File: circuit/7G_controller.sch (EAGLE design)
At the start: 21 parts, among them Q1 32768Hz, T1 TPS1101D

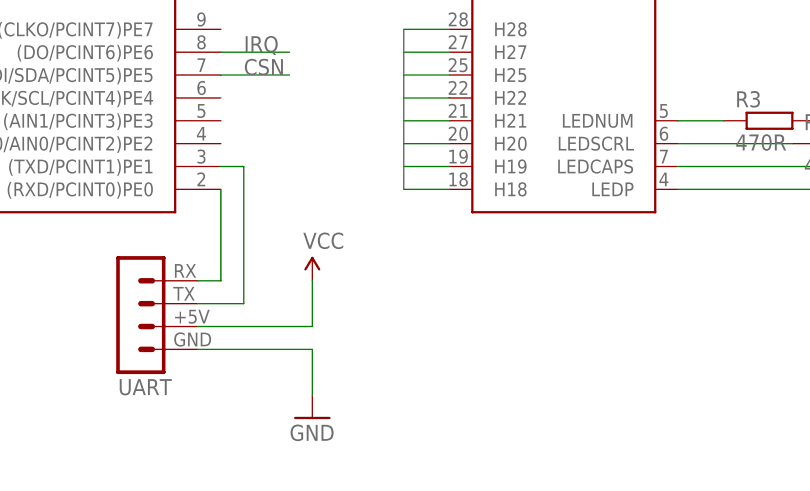
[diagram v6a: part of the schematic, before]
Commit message: 
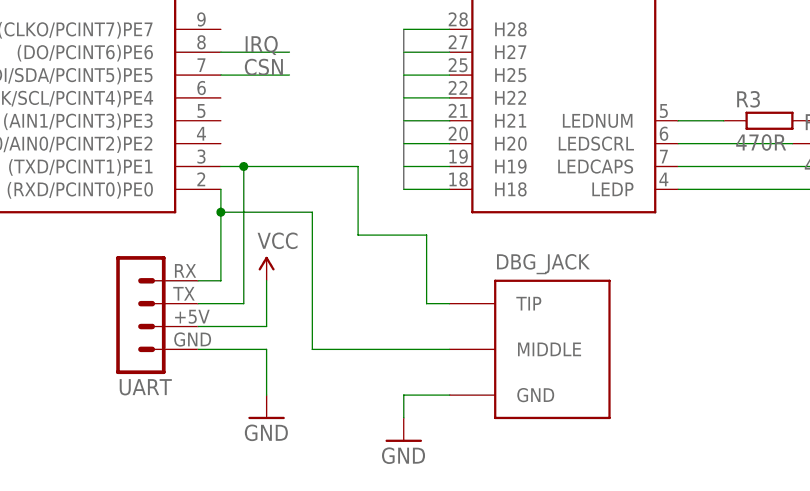
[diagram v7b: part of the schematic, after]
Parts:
- added DBG_JACK: JACK_FEMALE_3.5MMCHEAP, KileParts:JACK_FEMALE_3.5MMCHEAP
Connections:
- net GND: now also DBG_JACK.GND
- net N$29: now also DBG_JACK.MIDDLE
- net N$30: now also DBG_JACK.TIP
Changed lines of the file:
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@@
 <?xml version="1.0" encoding="utf-8"?>
 <!DOCTYPE eagle SYSTEM "eagle.dtd">
-<eagle version="6.4">
+<eagle version="6.5.0">
 <drawing>
 <settings>
@@
 <part name="SJ1" library="jumper" deviceset="SJ" device=""/>
 <part name="C7" library="rcl" deviceset="C-EU" device="C0805" value="100nF"/>
+<part name="DBG_JACK" library="KileParts" deviceset="JACK_FEMALE_3.5MM" device="CHEAP"/>
+<part name="GND6" library="SparkFun" deviceset="GND" device=""/>
 </parts>
 <sheets>
@@
 <instance part="P+7" gate="1" x="147.32" y="0"/>
 <instance part="UART" gate="1" x="43.18" y="-25.4" rot="MR180"/>
-<instance part="P+10" gate="1" x="63.5" y="-20.32"/>
-<instance part="GND7" gate="1" x="63.5" y="-35.56"/>
+<instance part="P+10" gate="1" x="58.42" y="-20.32"/>
+<instance part="GND7" gate="1" x="58.42" y="-35.56"/>
 <instance part="C5" gate="G$1" x="147.32" y="45.72"/>
 <instance part="R2" gate="G$1" x="132.08" y="-7.62"/>
@@
 <instance part="SJ1" gate="1" x="-86.36" y="35.56"/>
 <instance part="C7" gate="G$1" x="-22.86" y="81.28"/>
+<instance part="DBG_JACK" gate="G$1" x="91.44" y="-30.48"/>
+<instance part="GND6" gate="1" x="73.66" y="-38.1"/>
 </instances>
 <busses>
@@
 <segment>
 <pinref part="UART" gate="1" pin="TX"/>
-<wire x1="50.8" y1="-25.4" x2="63.5" y2="-25.4" width="0.1524" layer="91"/>
-<wire x1="63.5" y1="-25.4" x2="63.5" y2="-20.32" width="0.1524" layer="91"/>
+<wire x1="50.8" y1="-25.4" x2="58.42" y2="-25.4" width="0.1524" layer="91"/>
+<wire x1="58.42" y1="-25.4" x2="58.42" y2="-20.32" width="0.1524" layer="91"/>
 <pinref part="P+10" gate="1" pin="VCC"/>
 </segment>
@@
 <segment>
 <pinref part="UART" gate="1" pin="RX"/>
-<wire x1="50.8" y1="-27.94" x2="63.5" y2="-27.94" width="0.1524" layer="91"/>
-<wire x1="63.5" y1="-27.94" x2="63.5" y2="-33.02" width="0.1524" layer="91"/>
+<wire x1="50.8" y1="-27.94" x2="58.42" y2="-27.94" width="0.1524" layer="91"/>
+<wire x1="58.42" y1="-27.94" x2="58.42" y2="-33.02" width="0.1524" layer="91"/>
 <pinref part="GND7" gate="1" pin="GND"/>
 </segment>
@@
 <pinref part="GND8" gate="1" pin="GND"/>
 <wire x1="147.32" y1="38.1" x2="147.32" y2="40.64" width="0.1524" layer="91"/>
+</segment>
+<segment>
+<pinref part="DBG_JACK" gate="G$1" pin="GND"/>
+<wire x1="78.74" y1="-33.02" x2="73.66" y2="-33.02" width="0.1524" layer="91"/>
+<pinref part="GND6" gate="1" pin="GND"/>
+<wire x1="73.66" y1="-33.02" x2="73.66" y2="-35.56" width="0.1524" layer="91"/>
 </segment>
 </net>
@@
 <segment>
 <pinref part="ATMEGA169PV" gate="G$1" pin="(RXD/PCINT0)PE0"/>
-<wire x1="53.34" y1="-10.16" x2="53.34" y2="-20.32" width="0.1524" layer="91"/>
+<wire x1="53.34" y1="-10.16" x2="53.34" y2="-12.7" width="0.1524" layer="91"/>
 <pinref part="UART" gate="1" pin="GND"/>
+<wire x1="53.34" y1="-12.7" x2="53.34" y2="-20.32" width="0.1524" layer="91"/>
 <wire x1="50.8" y1="-20.32" x2="53.34" y2="-20.32" width="0.1524" layer="91"/>
+<pinref part="DBG_JACK" gate="G$1" pin="MIDDLE"/>
+<wire x1="78.74" y1="-27.94" x2="63.5" y2="-27.94" width="0.1524" layer="91"/>
+<wire x1="63.5" y1="-27.94" x2="63.5" y2="-12.7" width="0.1524" layer="91"/>
+<wire x1="63.5" y1="-12.7" x2="53.34" y2="-12.7" width="0.1524" layer="91"/>
+<junction x="53.34" y="-12.7"/>
 </segment>
 </net>
@@
 <pinref part="UART" gate="1" pin="+5V"/>
 <wire x1="55.88" y1="-22.86" x2="50.8" y2="-22.86" width="0.1524" layer="91"/>
-</segment>
-</net>
+<pinref part="DBG_JACK" gate="G$1" pin="TIP"/>
+<wire x1="78.74" y1="-22.86" x2="76.2" y2="-22.86" width="0.1524" layer="91"/>
+<wire x1="76.2" y1="-22.86" x2="76.2" y2="-15.24" width="0.1524" layer="91"/>
+<wire x1="76.2" y1="-15.24" x2="68.58" y2="-15.24" width="0.1524" layer="91"/>
+<wire x1="68.58" y1="-15.24" x2="68.58" y2="-7.62" width="0.1524" layer="91"/>
+<wire x1="68.58" y1="-7.62" x2="55.88" y2="-7.62" width="0.1524" layer="91"/>
+<junction x="55.88" y="-7.62"/>
+</segment>
+</net>
